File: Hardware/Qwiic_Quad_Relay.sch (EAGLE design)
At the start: 71 parts, among them J2 Qwiic Right Angle, J3 Qwiic Right Angle, J4 POWER_JACK, J9 AVR_SPI_PROG_3X2TESTPOINTS, K1 RELAY-SPDT-JZC-11F, K2 RELAY-SPDT-JZC-11F, K3 RELAY-SPDT-JZC-11F, K4 RELAY-SPDT-JZC-11F, Q1 600mA/40V, Q2 600mA/40V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

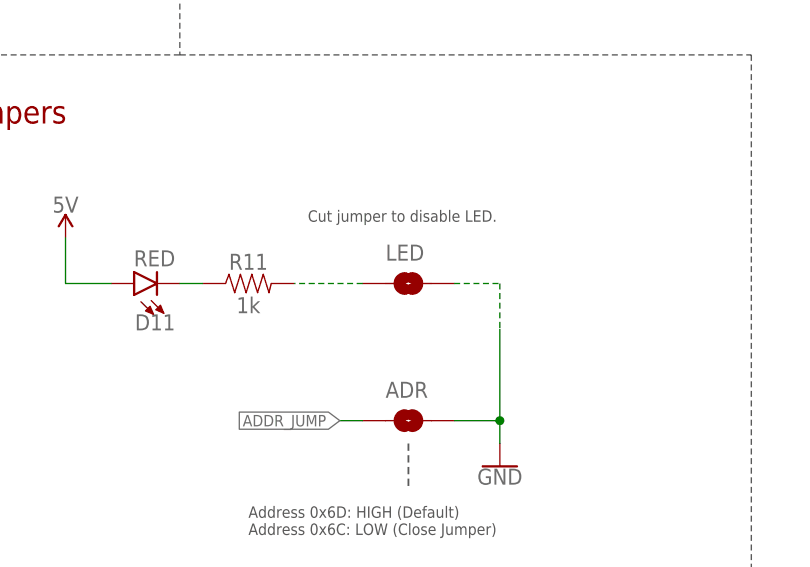
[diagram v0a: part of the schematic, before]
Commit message: Changes LED jumper to normally closed with trace
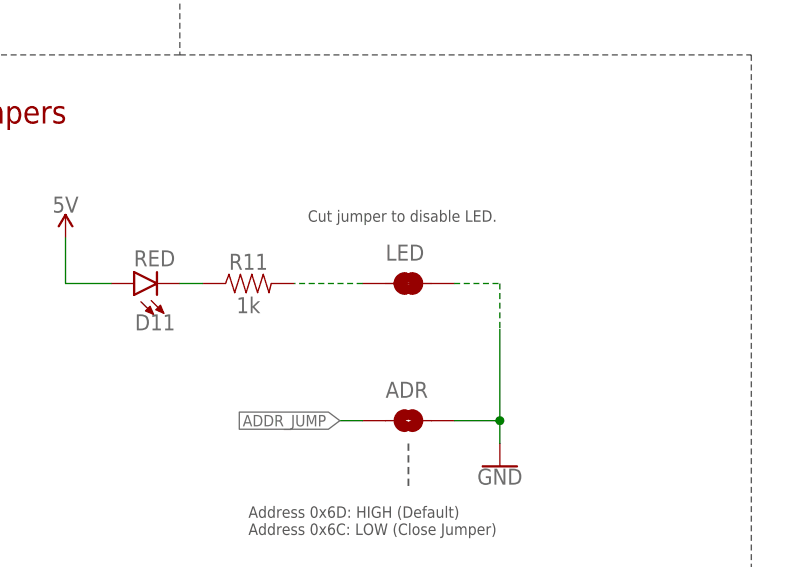
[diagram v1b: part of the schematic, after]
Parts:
- LED: value JUMPER-SMT_2_NO_SILK -> JUMPER-SMT_2_NC_TRACE_SILK; device SparkFun-Jumpers:JUMPER-SMT_2_NO_SILK -> SparkFun-Jumpers:JUMPER-SMT_2_NC_TRACE_SILK
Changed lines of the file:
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@@
 <?xml version="1.0" encoding="utf-8"?>
 <!DOCTYPE eagle SYSTEM "eagle.dtd">
-<eagle version="9.5.2">
+<eagle version="9.5.1">
 <drawing>
 <settings>
@@
 <part name="R5" library="SparkFun-Resistors" deviceset="12KOHM" device="-0603-1/10W-1%" value="12k"/>
 <part name="D6" library="SparkFun-DiscreteSemi" deviceset="DIODE-SCHOTTKY" device="-BAT60A" value="3A/10V/280mV"/>
-<part name="LED" library="SparkFun-Jumpers" deviceset="JUMPER-SMT_2_NO" device="_SILK" package3d_urn="urn:adsk.eagle:package:39279/1"/>
+<part name="LED" library="SparkFun-Jumpers" deviceset="JUMPER-SMT_2_NC_TRACE" device="_SILK" package3d_urn="urn:adsk.eagle:package:39281/1"/>
 <part name="BYP" library="SparkFun-Jumpers" deviceset="JUMPER-SMT_2_NO" device="_SILK" package3d_urn="urn:adsk.eagle:package:39279/1"/>
 <part name="GND7" library="SparkFun-PowerSymbols" deviceset="GND" device=""/>

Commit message: Replaces 33 Ohm resistors with 0 Ohm
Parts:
- R10, R2, R4, R8: value 33 -> 0; device SparkFun-Resistors:33OHM-0603-1/10W-1% -> SparkFun-Resistors:0OHM-0603-1/10W
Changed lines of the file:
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@@
 <part name="R16" library="SparkFun-Resistors" deviceset="330OHM" device="-0603-1/10W-1%" value="330"/>
 <part name="J3" library="SparkFun-Connectors" deviceset="I2C_STANDARD" device="QWIIC" value="Qwiic Right Angle"/>
-<part name="R2" library="SparkFun-Resistors" deviceset="33OHM" device="-0603-1/10W-1%" value="33"/>
+<part name="R2" library="SparkFun-Resistors" deviceset="0OHM" device="-0603-1/10W" value="0"/>
 <part name="JP4" library="SparkFun-Hardware" deviceset="STAND-OFF" device=""/>
 <part name="JP5" library="SparkFun-Hardware" deviceset="STAND-OFF" device=""/>
@@
 <part name="GND11" library="SparkFun-PowerSymbols" deviceset="GND" device=""/>
 <part name="GND12" library="SparkFun-PowerSymbols" deviceset="GND" device=""/>
-<part name="R4" library="SparkFun-Resistors" deviceset="33OHM" device="-0603-1/10W-1%" value="33"/>
-<part name="R8" library="SparkFun-Resistors" deviceset="33OHM" device="-0603-1/10W-1%" value="33"/>
-<part name="R10" library="SparkFun-Resistors" deviceset="33OHM" device="-0603-1/10W-1%" value="33"/>
+<part name="R4" library="SparkFun-Resistors" deviceset="0OHM" device="-0603-1/10W" value="0"/>
+<part name="R8" library="SparkFun-Resistors" deviceset="0OHM" device="-0603-1/10W" value="0"/>
+<part name="R10" library="SparkFun-Resistors" deviceset="0OHM" device="-0603-1/10W" value="0"/>
 <part name="D4" library="SparkFun-LED" deviceset="LED-BLUE" device="0603" value="BLUE"/>
 <part name="D7" library="SparkFun-LED" deviceset="LED-BLUE" device="0603" value="BLUE"/>

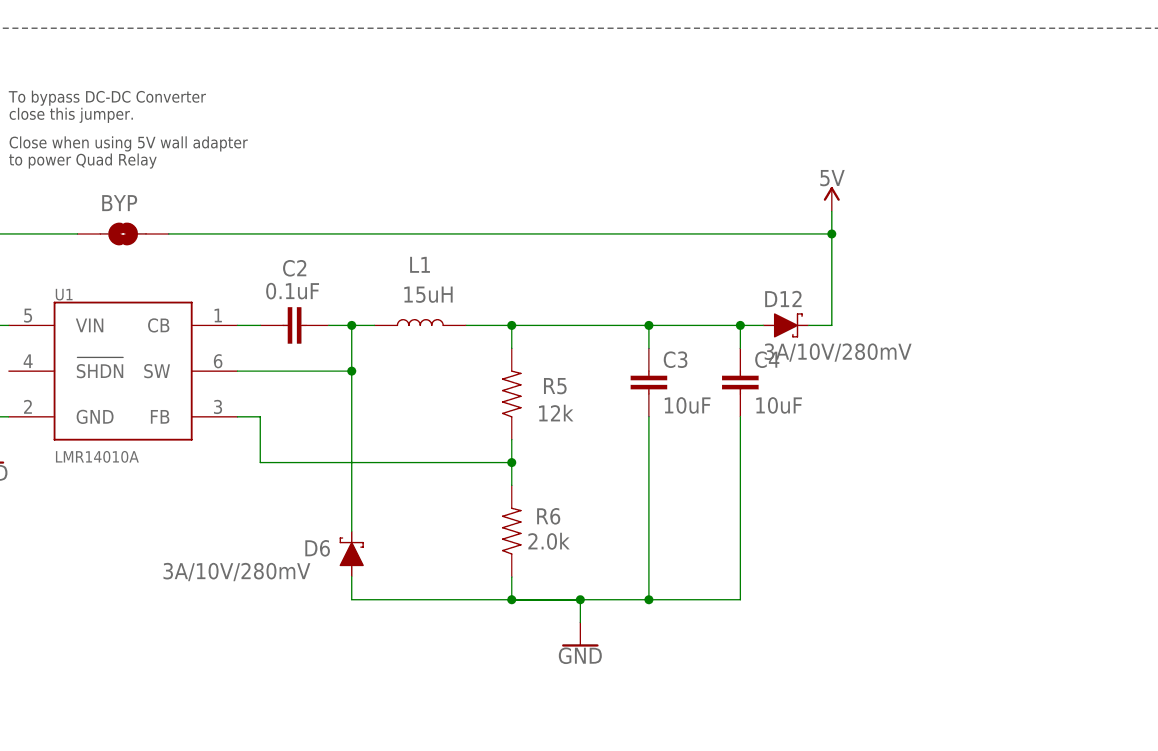
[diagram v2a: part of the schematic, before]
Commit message: Replaces clamping diode with something more suitable to stated maximum input voltage of the product.
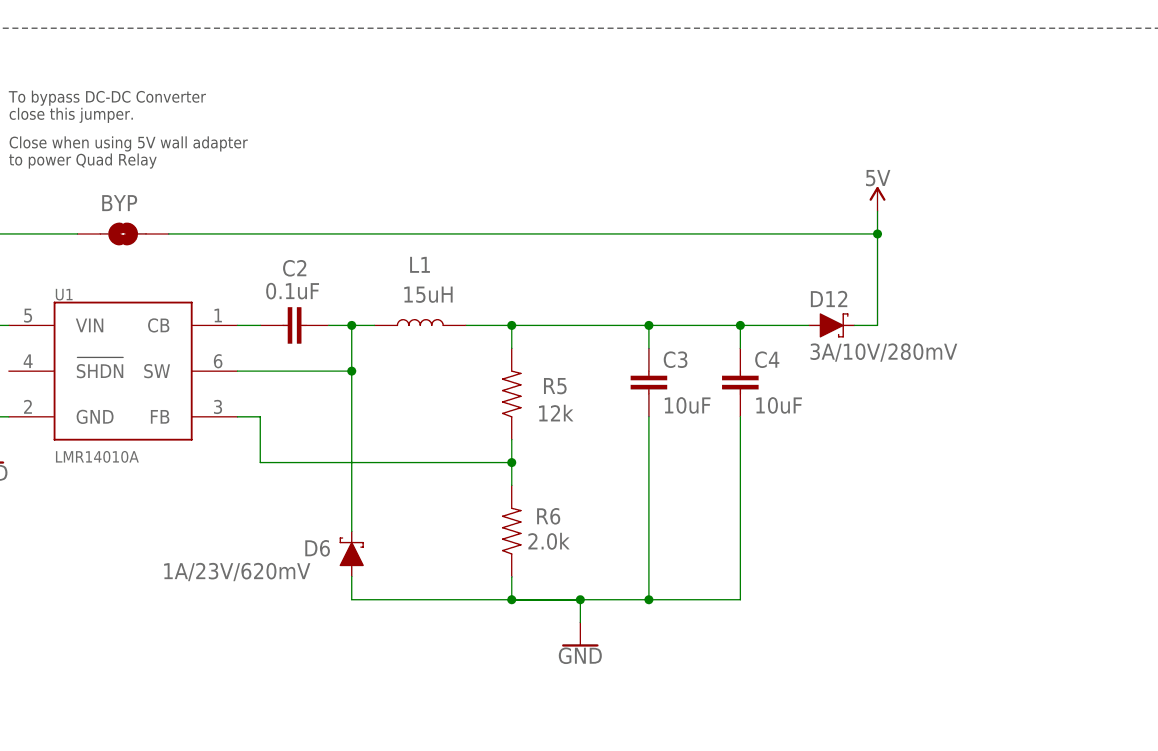
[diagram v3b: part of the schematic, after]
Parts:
- D6: value 3A/10V/280mV -> 1A/23V/620mV; device SparkFun-DiscreteSemi:DIODE-SCHOTTKY-BAT60A -> SparkFun-DiscreteSemi:DIODE-SCHOTTKY-BAT20J
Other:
- moved on the sheet: D12
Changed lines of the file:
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@@
 <?xml version="1.0" encoding="utf-8"?>
 <!DOCTYPE eagle SYSTEM "eagle.dtd">
-<eagle version="9.5.1">
+<eagle version="9.6.2">
 <drawing>
 <settings>
@@
 <layer number="56" name="wert" color="7" fill="1" visible="no" active="no"/>
 <layer number="57" name="tCAD" color="7" fill="1" visible="no" active="no"/>
+<layer number="58" name="bCAD" color="7" fill="1" visible="no" active="no"/>
 <layer number="59" name="tCarbon" color="7" fill="1" visible="no" active="no"/>
 <layer number="60" name="bCarbon" color="7" fill="1" visible="no" active="no"/>
@@
 <layer number="128" name="_bValues" color="7" fill="1" visible="yes" active="yes"/>
 <layer number="129" name="Mask" color="7" fill="1" visible="yes" active="yes"/>
+<layer number="130" name="SMDSTROOK" color="7" fill="1" visible="no" active="no"/>
 <layer number="131" name="tAdjust" color="7" fill="1" visible="yes" active="yes"/>
 <layer number="132" name="bAdjust" color="7" fill="1" visible="yes" active="yes"/>
+<layer number="133" name="bottom_silk" color="7" fill="1" visible="no" active="no"/>
+<layer number="134" name="silk_top" color="7" fill="1" visible="no" active="no"/>
+<layer number="135" name="silk_bottom" color="7" fill="1" visible="no" active="no"/>
+<layer number="136" name="silktop" color="7" fill="1" visible="no" active="no"/>
+<layer number="137" name="silkbottom" color="7" fill="1" visible="no" active="no"/>
+<layer number="138" name="EEE" color="7" fill="1" visible="no" active="no"/>
+<layer number="139" name="_tKeepout" color="7" fill="1" visible="no" active="no"/>
+<layer number="140" name="mbKeepout" color="7" fill="1" visible="no" active="no"/>
+<layer number="141" name="ASSEMBLY_TOP" color="7" fill="1" visible="no" active="no"/>
+<layer number="142" name="mbRestrict" color="7" fill="1" visible="no" active="no"/>
+<layer number="143" name="PLACE_BOUND_TOP" color="7" fill="1" visible="no" active="no"/>
 <layer number="144" name="Drill_legend" color="7" fill="1" visible="yes" active="yes"/>
+<layer number="145" name="DrillLegend_01-16" color="7" fill="1" visible="no" active="no"/>
+<layer number="146" name="DrillLegend_01-20" color="7" fill="1" visible="no" active="no"/>
+<layer number="147" name="PIN_NUMBER" color="7" fill="1" visible="no" active="no"/>
+<layer number="148" name="DrillLegend_01-20" color="7" fill="1" visible="no" active="no"/>
+<layer number="149" name="DrillLegend_02-15" color="7" fill="1" visible="no" active="no"/>
 <layer number="150" name="Notes" color="7" fill="1" visible="yes" active="yes"/>
 <layer number="151" name="HeatSink" color="7" fill="1" visible="yes" active="yes"/>
@@
 <layer number="154" name="FabDoc2" color="7" fill="1" visible="yes" active="yes"/>
 <layer number="155" name="FabDoc3" color="7" fill="1" visible="yes" active="yes"/>
+<layer number="156" name="gesam-Maß" color="1" fill="7" visible="no" active="no"/>
+<layer number="157" name="FaceMchng" color="3" fill="1" visible="no" active="no"/>
+<layer number="158" name="FaceMMeas" color="3" fill="1" visible="no" active="no"/>
+<layer number="159" name="Geh-Bear2" color="1" fill="7" visible="no" active="no"/>
+<layer number="160" name="Topologie" color="9" fill="1" visible="no" active="no"/>
+<layer number="161" name="tomplace2" color="7" fill="1" visible="no" active="no"/>
+<layer number="166" name="AntennaArea" color="7" fill="1" visible="no" active="no"/>
+<layer number="168" name="4mmHeightArea" color="7" fill="1" visible="no" active="no"/>
+<layer number="191" name="mNets" color="7" fill="1" visible="no" active="no"/>
+<layer number="192" name="mBusses" color="7" fill="1" visible="no" active="no"/>
+<layer number="193" name="mPins" color="7" fill="1" visible="no" active="no"/>
+<layer number="194" name="mSymbols" color="7" fill="1" visible="no" active="no"/>
+<layer number="195" name="mNames" color="7" fill="1" visible="no" active="no"/>
+<layer number="196" name="mValues" color="7" fill="1" visible="no" active="no"/>
 <layer number="199" name="Contour" color="7" fill="1" visible="yes" active="yes"/>
 <layer number="200" name="200bmp" color="1" fill="10" visible="yes" active="yes"/>
@@
 <layer number="250" name="Descript" color="3" fill="1" visible="no" active="no"/>
 <layer number="251" name="SMDround" color="12" fill="11" visible="no" active="no"/>
+<layer number="252" name="BR-BS" color="7" fill="1" visible="no" active="no"/>
+<layer number="253" name="Extra" color="7" fill="1" visible="no" active="no"/>
 <layer number="254" name="cooling" color="7" fill="1" visible="yes" active="yes"/>
 <layer number="255" name="routoute" color="7" fill="1" visible="yes" active="yes"/>
@@
 <part name="R6" library="SparkFun-Resistors" deviceset="2.0KOHM" device="-0603-1/10W-5%" value="2.0k"/>
 <part name="R5" library="SparkFun-Resistors" deviceset="12KOHM" device="-0603-1/10W-1%" value="12k"/>
-<part name="D6" library="SparkFun-DiscreteSemi" deviceset="DIODE-SCHOTTKY" device="-BAT60A" value="3A/10V/280mV"/>
+<part name="D6" library="SparkFun-DiscreteSemi" deviceset="DIODE-SCHOTTKY" device="-BAT20J" value="1A/23V/620mV"/>
 <part name="LED" library="SparkFun-Jumpers" deviceset="JUMPER-SMT_2_NC_TRACE" device="_SILK" package3d_urn="urn:adsk.eagle:package:39281/1"/>
 <part name="BYP" library="SparkFun-Jumpers" deviceset="JUMPER-SMT_2_NO" device="_SILK" package3d_urn="urn:adsk.eagle:package:39279/1"/>
@@
 </instance>
 <instance part="JP1" gate="G$1" x="685.8" y="27.94" smashed="yes"/>
-<instance part="D12" gate="G$1" x="449.58" y="152.4" smashed="yes">
-<attribute name="NAME" x="447.04" y="154.432" size="1.778" layer="95" font="vector"/>
-<attribute name="VALUE" x="447.04" y="150.368" size="1.778" layer="96" font="vector" align="top-left"/>
-</instance>
-<instance part="SUPPLY7" gate="G$1" x="454.66" y="165.1" smashed="yes">
-<attribute name="VALUE" x="454.66" y="167.894" size="1.778" layer="96" align="bottom-center"/>
+<instance part="D12" gate="G$1" x="454.66" y="152.4" smashed="yes">
+<attribute name="NAME" x="452.12" y="154.432" size="1.778" layer="95" font="vector"/>
+<attribute name="VALUE" x="452.12" y="150.368" size="1.778" layer="96" font="vector" align="top-left"/>
+</instance>
+<instance part="SUPPLY7" gate="G$1" x="459.74" y="165.1" smashed="yes">
+<attribute name="VALUE" x="459.74" y="167.894" size="1.778" layer="96" align="bottom-center"/>
 </instance>
 </instances>
@@
 <segment>
 <pinref part="D12" gate="G$1" pin="C"/>
-<wire x1="452.12" y1="152.4" x2="454.66" y2="152.4" width="0.1524" layer="91"/>
-<wire x1="454.66" y1="152.4" x2="454.66" y2="162.56" width="0.1524" layer="91"/>
+<wire x1="457.2" y1="152.4" x2="459.74" y2="152.4" width="0.1524" layer="91"/>
+<wire x1="459.74" y1="152.4" x2="459.74" y2="162.56" width="0.1524" layer="91"/>
 <pinref part="SUPPLY7" gate="G$1" pin="5V"/>
 <pinref part="BYP" gate="G$1" pin="2"/>
-<wire x1="454.66" y1="162.56" x2="454.66" y2="165.1" width="0.1524" layer="91"/>
-<wire x1="381" y1="162.56" x2="454.66" y2="162.56" width="0.1524" layer="91"/>
-<junction x="454.66" y="162.56"/>
+<wire x1="459.74" y1="162.56" x2="459.74" y2="165.1" width="0.1524" layer="91"/>
+<wire x1="381" y1="162.56" x2="459.74" y2="162.56" width="0.1524" layer="91"/>
+<junction x="459.74" y="162.56"/>
 </segment>
 </net>
@@
 <junction x="419.1" y="152.4"/>
 <pinref part="D12" gate="G$1" pin="A"/>
-<wire x1="447.04" y1="152.4" x2="444.5" y2="152.4" width="0.1524" layer="91"/>
+<wire x1="452.12" y1="152.4" x2="444.5" y2="152.4" width="0.1524" layer="91"/>
 <junction x="444.5" y="152.4"/>
 </segment>

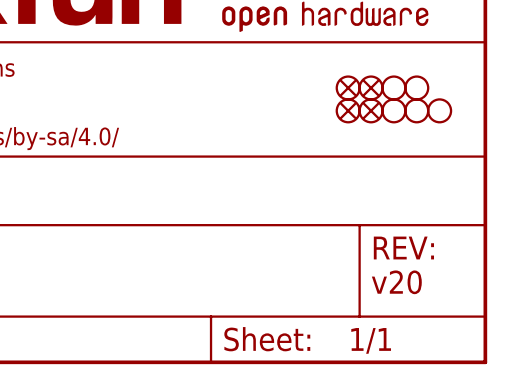
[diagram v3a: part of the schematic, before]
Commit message: Rolls version in schematic to v21
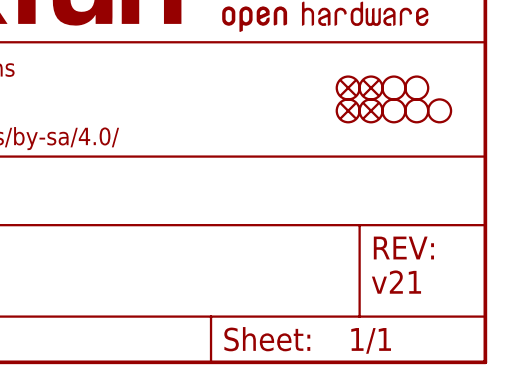
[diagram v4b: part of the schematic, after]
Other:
- note added: "v21"
- note removed: "v20"
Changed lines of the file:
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@@
 <plain>
 <text x="607.06" y="7.62" size="2.54" layer="94" font="vector">Elias Santistevan</text>
-<text x="678.18" y="7.62" size="2.54" layer="94" font="vector">v20</text>
+<text x="678.18" y="7.62" size="2.54" layer="94" font="vector">v21</text>
 <text x="266.7" y="271.78" size="2.54" layer="94" font="vector">Relay Control</text>
 <text x="266.7" y="86.36" size="2.54" layer="94" font="vector">Connectors</text>
